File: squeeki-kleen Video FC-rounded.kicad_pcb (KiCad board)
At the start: 2 copper layers, 50.8 x 17.8 mm, 49 parts, among them J1 VCC, J2 VOUT, J3 GND, J4 Conn_Coaxial, Q1 MMBT3906

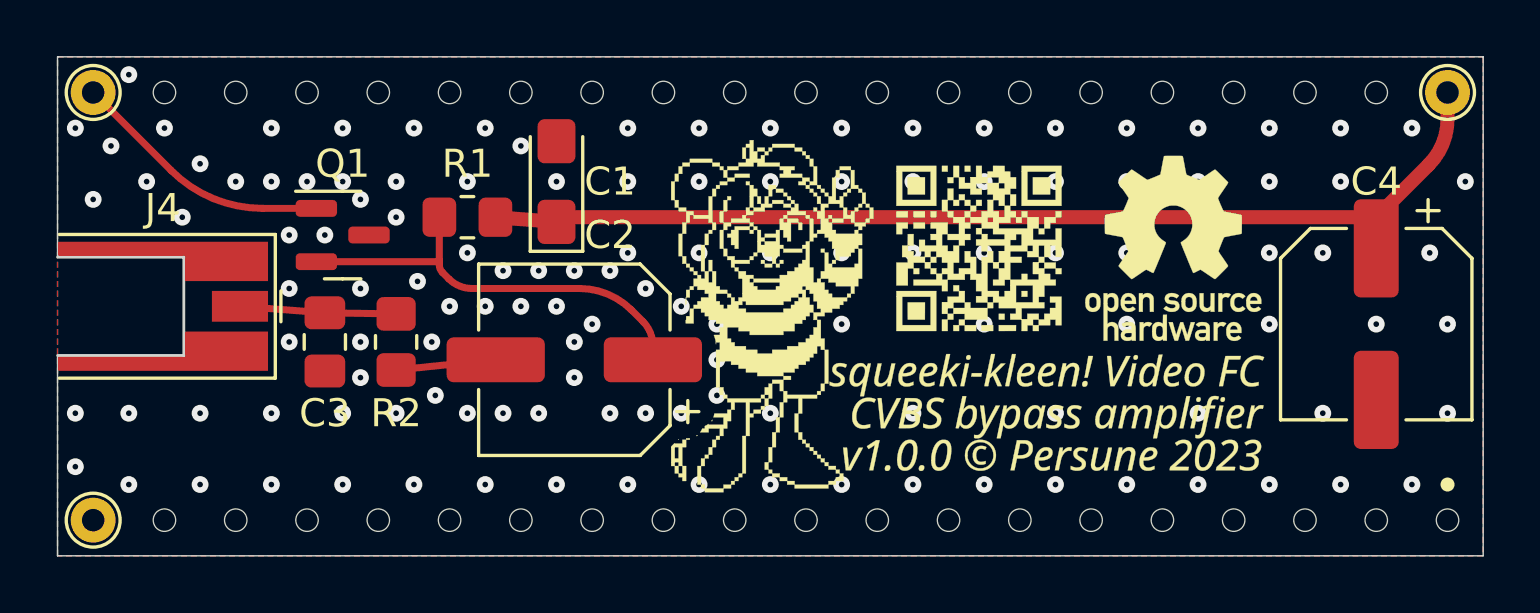
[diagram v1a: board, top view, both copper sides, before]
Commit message: Compact component placement, add teardrops
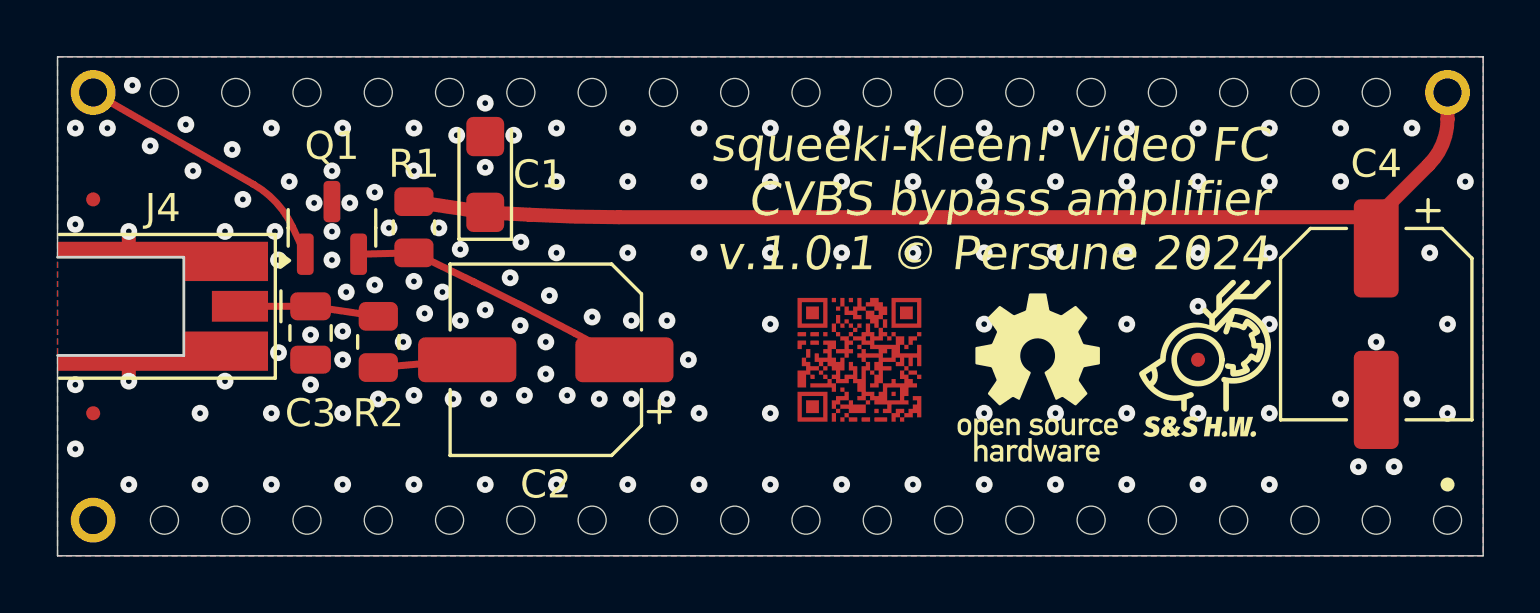
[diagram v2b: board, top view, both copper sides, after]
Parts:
- removed Ref**: Val**, custom footprints:squeeki-kleen Video FC-rounded-brd
- added REF**: Fiducial_0.5mm_Mask1.5mm, Fiducial:Fiducial_0.5mm_Mask1.5mm, F.Cu at (79.4, 37.5)
- added REF**: Fiducial_0.5mm_Mask1.5mm, Fiducial:Fiducial_0.5mm_Mask1.5mm, F.Cu at (40.0, 39.4)
- added REF**: Fiducial_0.5mm_Mask1.5mm, Fiducial:Fiducial_0.5mm_Mask1.5mm, F.Cu at (40.0, 31.8)
- added svg2mod: G***, custom footprints:qr, F.Cu at (67.3, 37.5)
- added svg2mod: G***, custom footprints:maustech icon fiducial 0-50mm 1-50mm, F.Cu at (79.4, 37.5)
- added svg2mod: G***, custom footprints:oshw-logo 6x6mm, F.Cu at (73.7, 38.1)
- C1: footprint Capacitor_Tantalum_SMD:CP_EIA-3216-18_Kemet-A_Pad1.58x1.35mm_HandSolder -> Capacitor_Tantalum_SMD:CP_EIA-3216-18_Kemet-A
- C3: footprint Capacitor_SMD:C_0805_2012Metric_Pad1.18x1.45mm_HandSolder -> Capacitor_SMD:C_0805_2012Metric
- R1, R2: footprint Resistor_SMD:R_0805_2012Metric_Pad1.20x1.40mm_HandSolder -> Resistor_SMD:R_0805_2012Metric
- moved C1 2.55 mm to (54.0, 30.9)
- moved R1 1.94 mm to (51.4, 32.7), turned to 90 degrees
- moved C2 1.02 mm to (56.1, 37.5)
- moved R2 0.63 mm to (50.2, 36.8)
- moved C3 0.60 mm to (47.8, 36.5)
- moved Q1 0.46 mm to (48.5, 32.8), turned to 90 degrees
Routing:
- net Net-(Q1-E): track 15.5 -> 10.4 mm
- net VCC: track 37.9 -> 39.7 mm
- net GND: track 0.00 -> 0.76 mm, vias 129 -> 145
- net /CVBS: track 5.57 -> 4.96 mm
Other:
- board text added: "squeeki-kleen! Video FC CVBS bypass amplifier v.1.0.1 © Persune 2024"

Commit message: Widen holes, add extra empty capacitor footprints
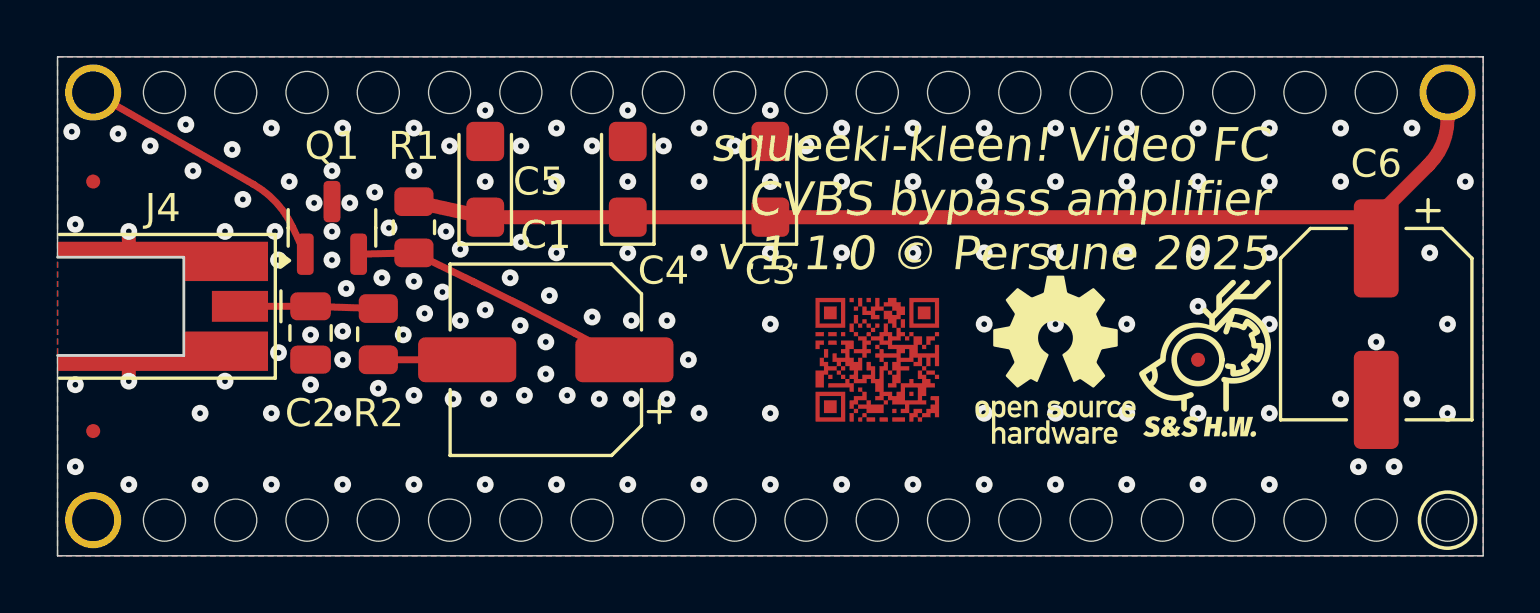
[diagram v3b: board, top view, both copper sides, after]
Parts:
- added C3: ~, Capacitor_Tantalum_SMD:CP_EIA-3216-18_Kemet-A, F.Cu at (64.1, 31.0)
- added C4: ~, Capacitor_Tantalum_SMD:CP_EIA-3216-18_Kemet-A, F.Cu at (59.1, 31.0)
- moved svg2mod 0.90 mm to (74.3, 37.5)
- moved REF** 0.64 mm to (40.0, 40.0)
- moved REF** 0.64 mm to (40.0, 31.1)
- moved svg2mod 0.63 mm to (67.9, 37.5)
- moved R2 0.28 mm to (50.2, 36.6)
- moved C5 0.17 mm to (54.0, 31.0)
- renumbered C2 to C1, C3 to C2, C1 to C5, C4 to C6
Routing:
- net GND: vias 145 -> 148
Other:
- board text added: "squeeki-kleen! Video FC CVBS bypass amplifier v.1.1.0 © Persune 2025"
- board text removed: "squeeki-kleen! Video FC CVBS bypass amplifier v.1.0.1 © Persune 2024"
